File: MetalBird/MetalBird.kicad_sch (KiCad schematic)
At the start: 14 parts, among them SW1 SW_Push_Open, U1 STM32F411CEUx, Y1 8MHz

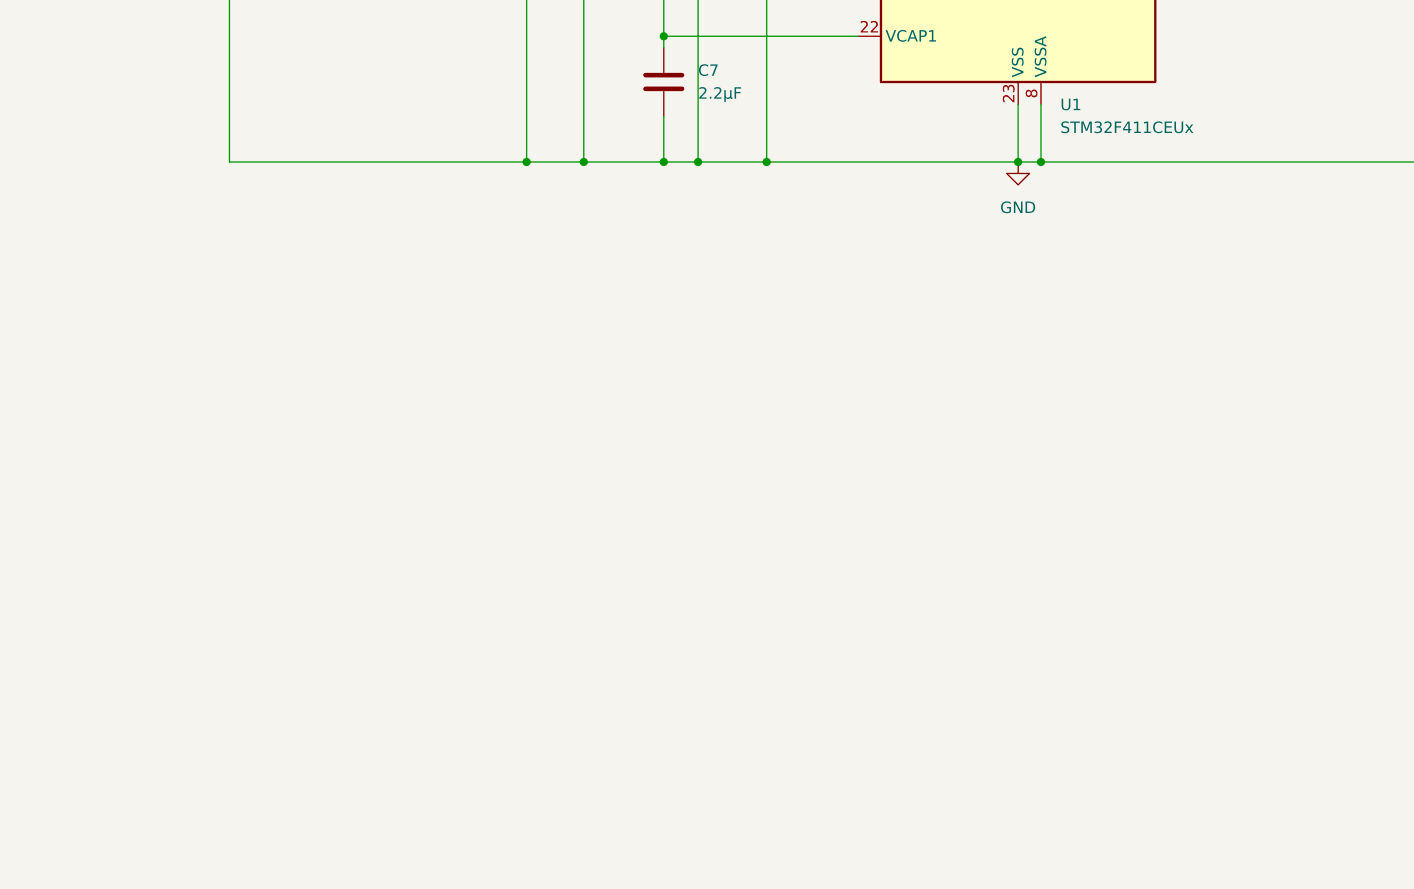
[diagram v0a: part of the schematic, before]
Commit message: Buck Converter Setup (7.4 V -> 5.4 V)
Values of resistors, capacitors, inductors calculated by taking reference from manual.
Manual: https://www.monolithicpower.com/en/documentview/productdocument/index/version/2/document_type/Datasheet/lang/en/sku/MP2331HGTL-Z/
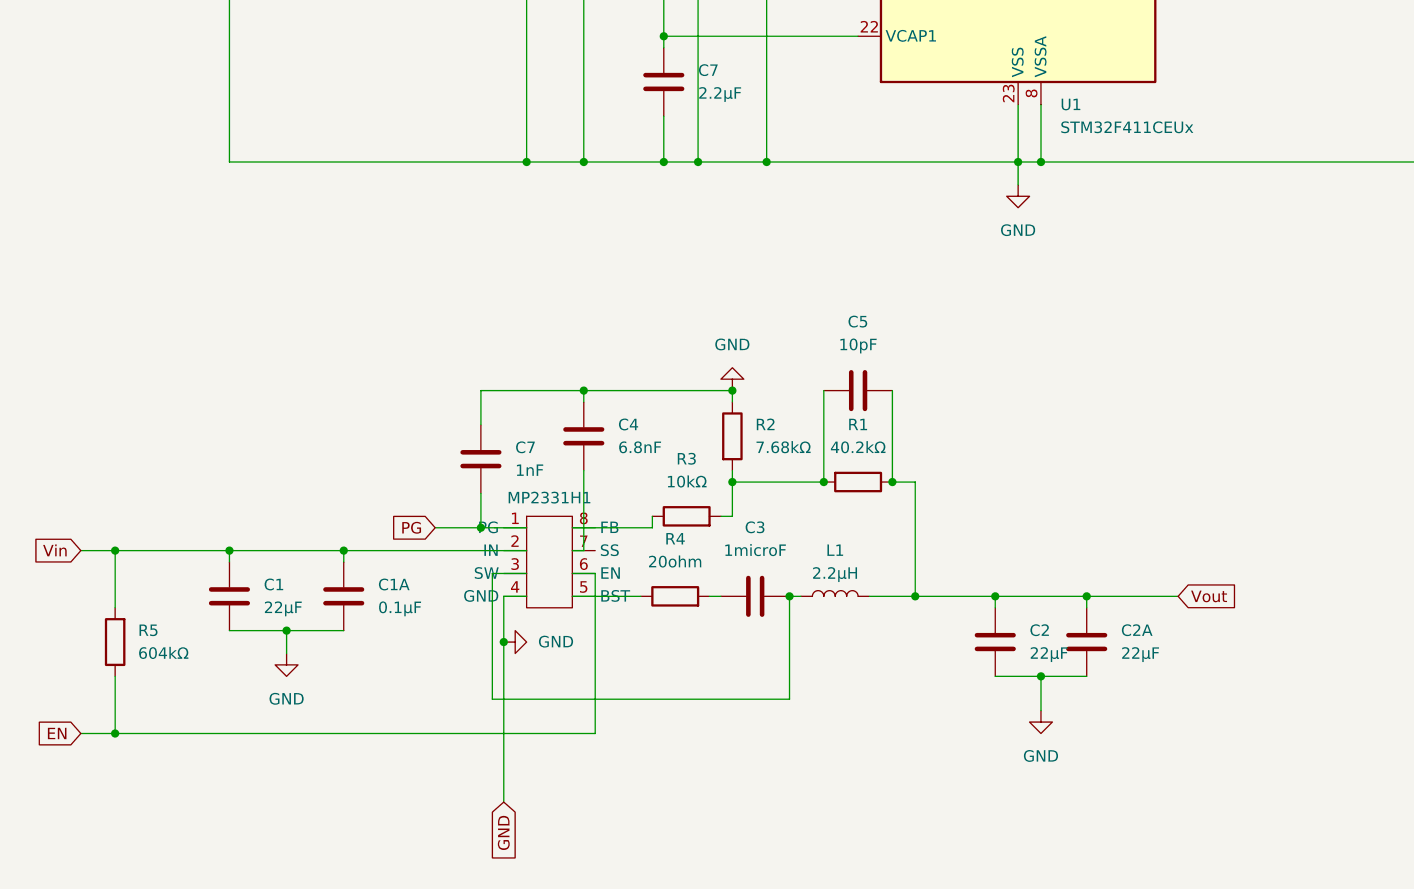
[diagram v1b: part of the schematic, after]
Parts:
- added C1, C2, C2A: 22µF, symbol Device:C
- added C1A: 0.1µF, symbol Device:C
- added C3: 1microF, symbol Device:C
- added C4: 6.8nF, symbol Device:C
- added C5: 10pF, symbol Device:C
- added C7: 1nF, symbol Device:C
- added L1: 2.2µH, symbol Device:L
- added MP2331H1: ~, symbol Metal_bird_library:MP2331H
- added R1: 40.2kΩ, symbol Device:R
- added R2: 7.68kΩ, symbol Device:R
- added R3: 10kΩ, symbol Device:R
- added R4: 20ohm, symbol Device:R
- added R5: 604kΩ, symbol Device:R
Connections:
- net GND: now also C1.1, C1A.1, C2.2, C2A.2, C4.2, C7.2, MP2331H1.4 (GND), R2.1
- new net: C3.2, L1.1, MP2331H1.3 (SW)
- new net: MP2331H1.5 (BST), R4.1
- new net: C3.1, R4.2
- new net: C5.1, R1.2, R2.2, R3.2
- new net: C4.1, MP2331H1.7 (SS)
- new net: MP2331H1.8 (FB), R3.1
- new net EN: MP2331H1.6 (EN), R5.1
- new net PG: C7.1, MP2331H1.1 (PG)
- new net Vin: C1.2, C1A.2, MP2331H1.2 (IN), R5.2
- new net Vout: C2.1, C2A.1, C5.2, L1.2, R1.1

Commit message: LDO setup
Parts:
- added C10: 22µF, symbol Device:C
- added U2: AMS1117-3.3, Package_TO_SOT_SMD:SOT-223-3_TabPin2, symbol Regulator_Linear:AMS1117-3.3
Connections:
- net GND: now also C10.2, U2.1 (GND)
- net Vin renamed Vin (7.4 V)
- net Vout renamed Vout (5 V)
- new net Vin (5 V): U2.3 (VI)
- new net Vout (3.3 V): C10.1, U2.2 (VO)

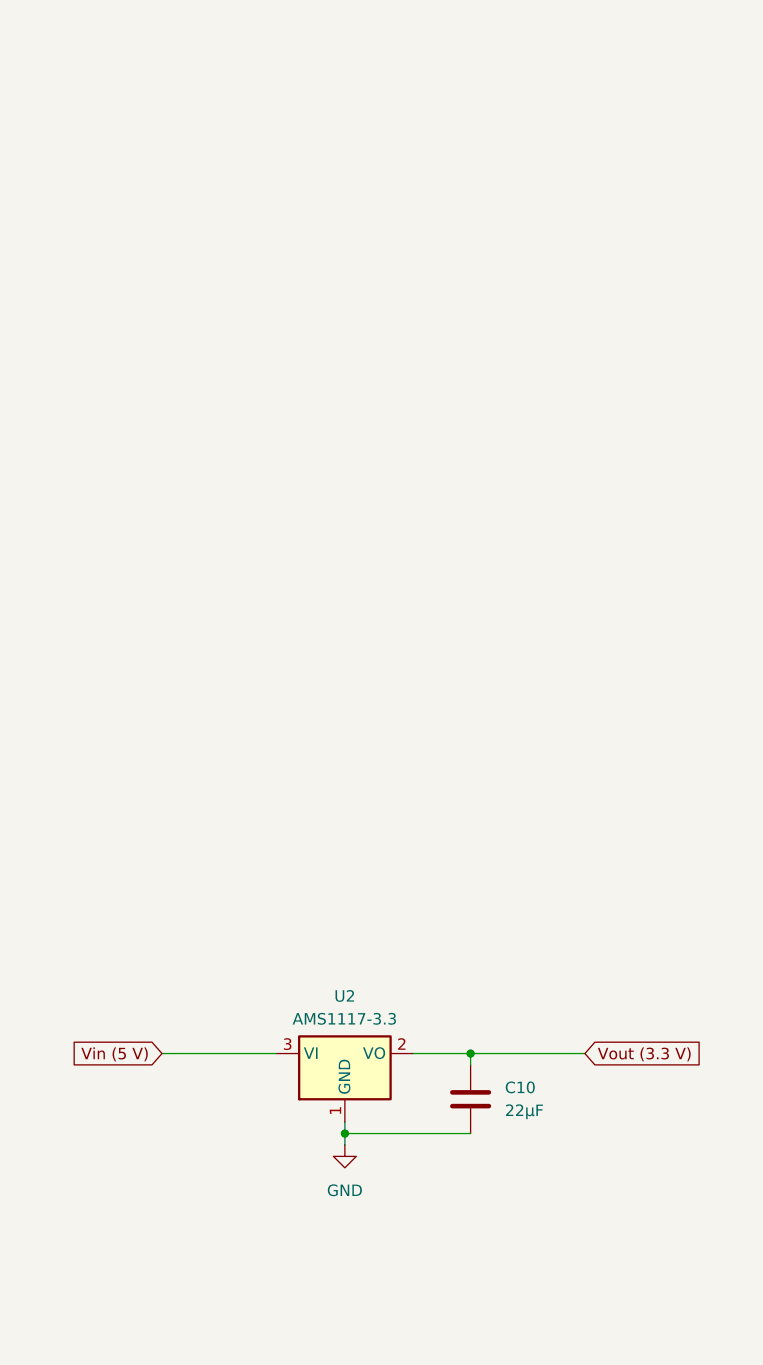
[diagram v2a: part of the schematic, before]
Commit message: IMU Schematic
+ LDO decoupling capacitor
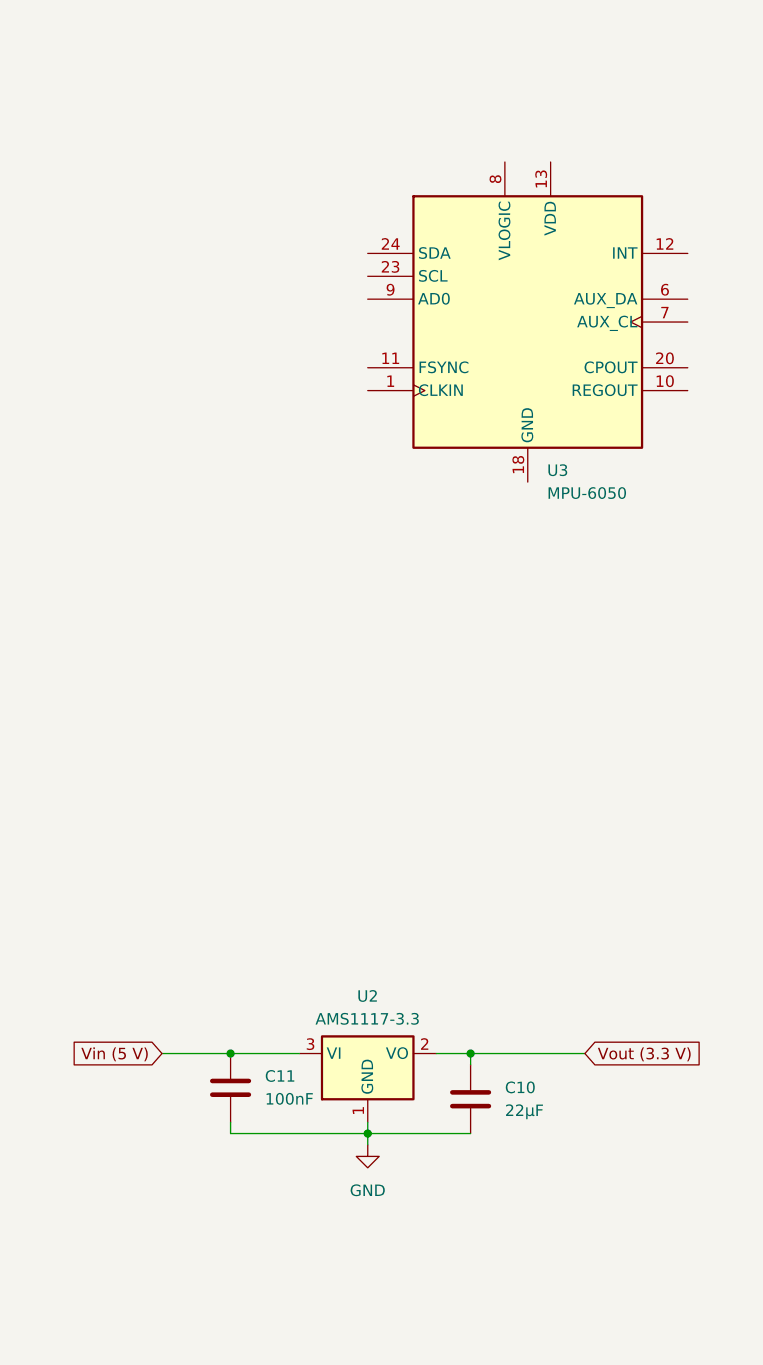
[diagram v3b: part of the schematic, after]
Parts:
- added C11: 100nF, symbol Device:C
- added U3: MPU-6050, Sensor_Motion:InvenSense_QFN-24_4x4mm_P0.5mm, symbol Sensor_Motion:MPU-6050
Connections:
- net GND: now also C11.2
- net Vin (5 V): now also C11.1
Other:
- moved on the sheet: U2

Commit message: IMU Complete
Used MPU-6050 Product specification datasheet for reference
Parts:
- added C12: 2.2 nF, symbol Device:C
- added C13, C15: 0.1 microF, symbol Device:C
- added C14: 10 nF, symbol Device:C
- added R6, R7, R8: 4.7 K, symbol Device:R
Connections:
- net GND: now also U3.1 (CLKIN), U3.11 (FSYNC), U3.18 (GND), U3.9 (AD0), C12.2, C13.2, C14.1, C15.1
- net at U3.10 (REGOUT): now also C13.1
- net INT: now reaches U3.12 (INT)
- net INT: now also U1.40 (PB4), R8.1
- net 3.3 V: now reaches U3.13 (VDD)
- net 3.3 V: now also U3.8 (VLOGIC), C14.2, C15.2, R6.1, R7.1, R8.2
- net at U3.20 (CPOUT): now also C12.1
- net SCL: now reaches U3.23 (SCL)
- net SCL: now also U1.21 (PB10), R7.2
- net SDA: now reaches U3.24 (SDA)
- net SDA: now also U1.39 (PB3), R6.2
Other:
- moved on the sheet: U3

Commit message: Flight Controller Schematic Complete
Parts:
- removed R6, R7: 4.7 K, symbol Device:R
- added C22, C23, C25: 100nF, symbol Device:C
- added C24: 1000microF, symbol Device:C_Polarized
- added D1, D2: LED, symbol Device:LED
- added J1: Battery Conn, symbol Connector_Generic:Conn_01x02
- added J10: VTX Conn, symbol Connector_Generic:Conn_01x03
- added J2: SWD, symbol Connector_Generic:Conn_01x04
- added J3: ESC1, symbol Connector_Generic:Conn_01x03
- added J4: ESC2, symbol Connector_Generic:Conn_01x03
- added J5: ESC3, symbol Connector_Generic:Conn_01x03
- added J6: ESC4, symbol Connector_Generic:Conn_01x03
- added J7: ELRS Reciver, symbol Connector_Generic:Conn_01x04
- added J8: USB/UART DEBUG, symbol Connector_Generic:Conn_01x04
- added J9: Camera Conn, symbol Connector_Generic:Conn_01x03
- added Q1: PMOS, symbol Simulation_SPICE:PMOS
- added R11: 30.9K, symbol Device:R
- added R12: 20K, symbol Device:R
- added R13, R14: 150, symbol Device:R
- added R15, R16, R17: 4.7 K, symbol Device:R
- added U4: BMP280, Package_LGA:Bosch_LGA-8_2x2.5mm_P0.65mm_ClockwisePinNumbering, symbol Sensor_Pressure:BMP280
- R8: value 4.7 K -> 10K
- renumbered C8 to C10, C3 to C11, C9 to C12, C5 to C13, C2 to C14, C6 to C15, C11 to C16, C14 to C17, C15 to C18, C10 to C19, C1A to C1A1, C1 to C2, C13 to C20, C12 to C21, C2A to C2A1, C2 to C3, C3 to C4, C7 to C5, C4 to C6, C4 to C7, C5 to C8, C7 to C9, R5 to R1, R1 to R2, R4 to R3, R3 to R4, R2 to R5, R2 to R6, R1 to R7
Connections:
- net Vout (3.3 V) is gone; now on net 3.3V: C19.1, U2.2 (VO)
- net Vout (5 V) is gone; now on net 5V: C13.2, C14.1, C2A1.1, L1.2, R7.1
- net GND: now also C10.1, C12.1, R2.1, R8.2, C22.2, C23.2, C24.2, C25.2, D1.1 (K), D2.1 (K), J1.2 (Pin_2), J10.2 (Pin_2), J2.4 (Pin_4), J3.1 (Pin_1), J4.1 (Pin_1), J5.1 (Pin_1), J6.1 (Pin_1), J7.2 (Pin_2), J8.2 (Pin_2), J9.2 (Pin_2), R12.2, U4.1 (GND), U4.7 (GND); no longer C10.2, C12.2, R2.2
- net INT: now also R16.2; no longer R8.1
- net SCL: now also R17.2, U4.4 (SCK)
- net SDA: now also R15.2, U4.3 (SDI)
- net at U1.6 (PH1), Y1.1: now also C12.2; no longer C12.1
- net at U1.5 (PH0), Y1.2: now also C10.2; no longer C10.1
- net 3.3V: now reaches U1.1 (VBAT)
- net 3.3V: now also C1.1, C15.2, C17.2, C18.2, C3.1, C4.1, C6.1, C8.1, R6.1, U1.24 (VDD), U1.36 (VDD), U1.48 (VDD), U1.9 (VDDA), U3.13 (VDD), U3.8 (VLOGIC), C22.1, C23.1, J2.1 (Pin_1), R15.1, R16.1, R17.1, U4.2 (CSB), U4.5 (SDO), U4.6 (VDDIO), U4.8 (VDD)
- net at U1.11 (PA1): now also C25.1, R11.2, R12.1
- net USART2_TX: now reaches U1.12 (PA2)
- net USART2_TX: now also J7.3 (Pin_3)
- net USART2_RX: now reaches U1.13 (PA3)
- net USART2_RX: now also J7.4 (Pin_4)
- net at U1.26 (PB13): now also R13.2
- net at U1.27 (PB14): now also R14.2
- net at U1.29 (PA8): now also J3.3 (Pin_3)
- net at U1.30 (PA9): now also J4.3 (Pin_3)
- net at U1.31 (PA10): now also J5.3 (Pin_3)
- net at U1.32 (PA11): now also J6.3 (Pin_3)
- net SWDIO: now reaches U1.34 (PA13)
- net SWDIO: now also J2.2 (Pin_2)
- net SWDCLK: now reaches U1.37 (PA14)
- net SWDCLK: now also J2.3 (Pin_3)
- net USART1_TX: now reaches U1.42 (PB6)
- net USART1_TX: now also J8.3 (Pin_3)
- net USART1_RX: now reaches U1.43 (PB7)
- net USART1_RX: now also J8.4 (Pin_4)
- net at U1.44 (BOOT0): now also R2.2; no longer R2.1
- removed net +3.3V: C1.1, C15.2, C3.1, C4.1, C6.1, C8.1, C9.1, R6.1, U1.22 (VCAP1), U1.24 (VDD), U1.36 (VDD), U1.48 (VDD), U1.9 (VDDA)
- removed net 3.3 V: C17.2, C18.2, R8.2, U3.13 (VDD), U3.8 (VLOGIC)
- net EN: no longer names the net of MP2331H1.6 (EN), R1.1
- net PG: no longer names the net of C5.1, MP2331H1.1 (PG)
- net Vin (5 V) renamed 5V
- net 5V: now also J10.1 (Pin_1), J3.2 (Pin_2), J4.2 (Pin_2), J5.2 (Pin_2), J6.2 (Pin_2), J7.1 (Pin_1), J8.1 (Pin_1), J9.1 (Pin_1)
- net Vin (7.4 V) renamed 7.4V
- net 7.4V: now also R8.1, C24.1, Q1.1 (D), Q1.2 (G), R11.1
- new net: C9.1, U1.22 (VCAP1)
- new net: D1.2 (A), R13.1
- new net: J1.1 (Pin_1), Q1.3 (S)
- new net: D2.2 (A), R14.1
- new net Video: J10.3 (Pin_3), J9.3 (Pin_3)
- no-connect marks 0 -> 20
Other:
- moved on the sheet: C1, C10, C11, C12, C13, C14, C16, C17, C18, C19, C1A1, C2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
